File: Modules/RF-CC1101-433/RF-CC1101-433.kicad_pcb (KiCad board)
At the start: 4 copper layers, 25 parts, among them J3 SMA edge-mount 50R, U4 CC1101RGPR, Y2 26.000MHz CL=10pF

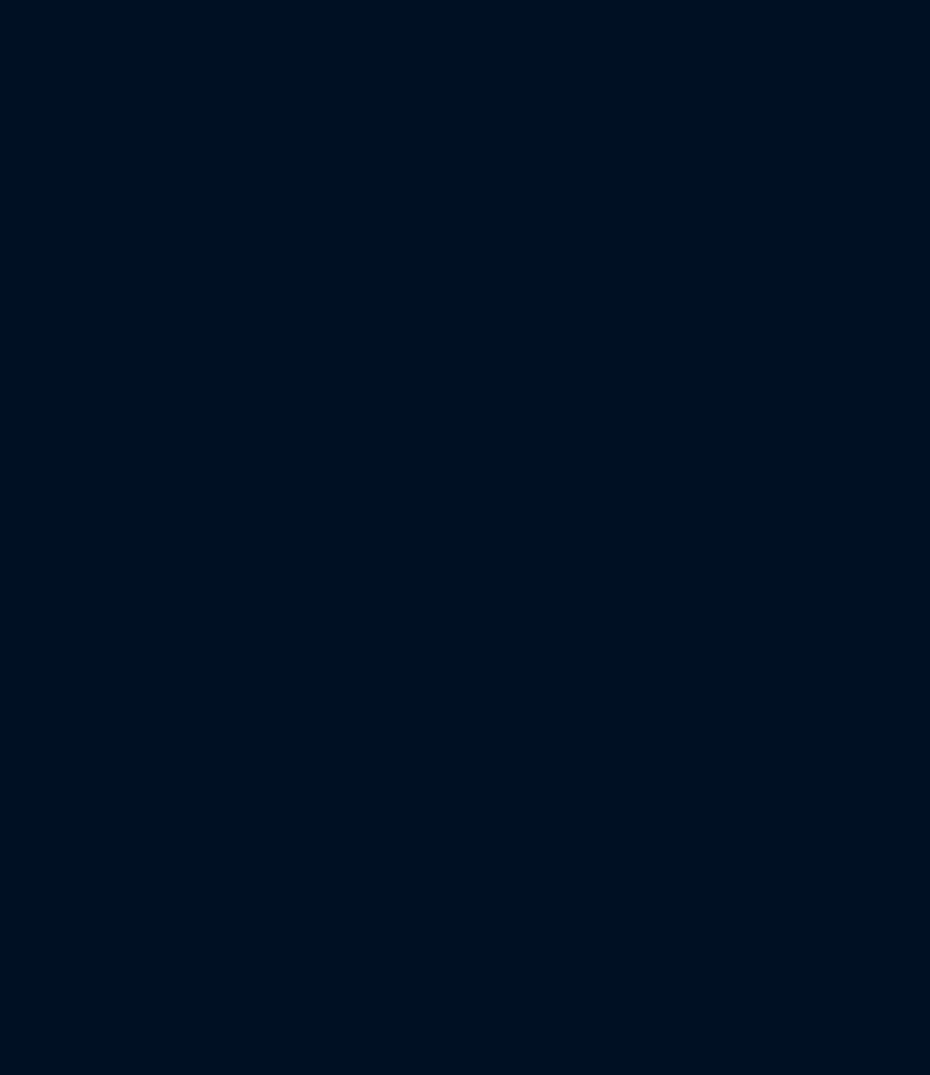
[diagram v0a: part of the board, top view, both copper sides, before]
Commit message: Add the base zones to five module boards
Whole-board zones for USBC, Buck, PowerMux, MCU and RF, written by file
before each board is opened. RF In1 carries a notch under J3 pad 1. Power
polygons become wide tracks during layout, because add_copper_pour cannot
set a zone priority.

Co-Authored-By: Claude Opus 5.5 (1M context) <noreply@anthropic.com>
Claude-Session: https://claude.ai/code/session_01ErAAfkmF4h3T5yfrw21utF
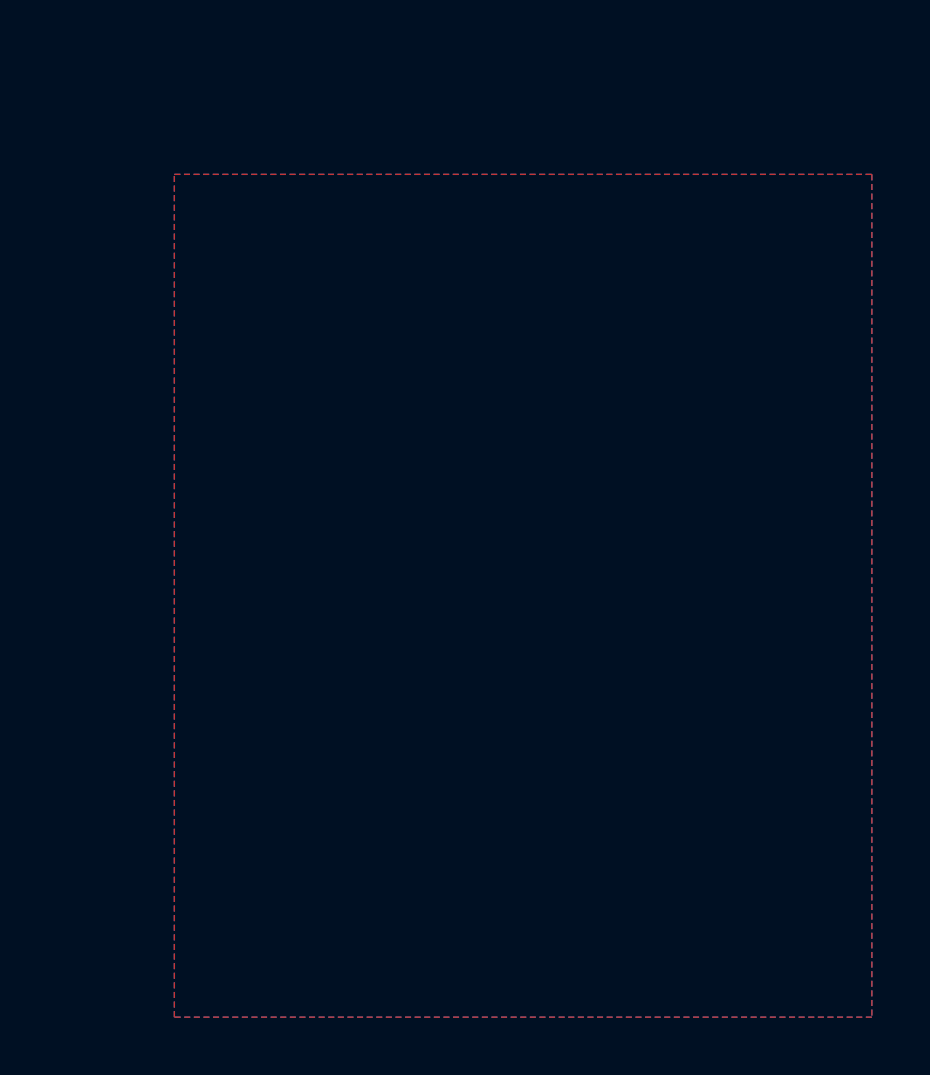
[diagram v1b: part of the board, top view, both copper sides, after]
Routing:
- added copper zone on B.Cu, net GND
- added copper zone on F.Cu, net GND
- added copper zone on In1.Cu, net GND
- added copper zone on In2.Cu, net GND
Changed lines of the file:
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@@
 	)
 	(embedded_fonts no)
-)
+  (zone (net 0) (net_name "GND") (layer "F.Cu")
+    (hatch edge 0.508)
+    (connect_pads (clearance 0.2))
+    (min_thickness 0.25)
+    (fill yes)
+    (polygon (pts
+      (xy 100.5 100.5)
+      (xy 124.5 100.5)
+      (xy 124.5 129.5)
+      (xy 100.5 129.5)
+    ))
+  )
+  (zone (net 0) (net_name "GND") (layer "In1.Cu")
+    (hatch edge 0.508)
+    (connect_pads (clearance 0.2))
+    (min_thickness 0.25)
+    (fill yes)
+    (polygon (pts
+      (xy 100.5 100.5)
+      (xy 110.38 100.5)
+      (xy 110.38 105.33)
+      (xy 112.38 105.33)
+      (xy 112.38 100.5)
+      (xy 124.5 100.5)
+      (xy 124.5 129.5)
+      (xy 100.5 129.5)
+    ))
+  )
+  (zone (net 0) (net_name "GND") (layer "In2.Cu")
+    (hatch edge 0.508)
+    (connect_pads (clearance 0.2))
+    (min_thickness 0.25)
+    (fill yes)
+    (polygon (pts
+      (xy 100.5 100.5)
+      (xy 124.5 100.5)
+      (xy 124.5 129.5)
+      (xy 100.5 129.5)
+    ))
+  )
+  (zone (net 0) (net_name "GND") (layer "B.Cu")
+    (hatch edge 0.508)
+    (connect_pads (clearance 0.2))
+    (min_thickness 0.25)
+    (fill yes)
+    (polygon (pts
+      (xy 100.5 100.5)
+      (xy 124.5 100.5)
+      (xy 124.5 129.5)
+      (xy 100.5 129.5)
+    ))
+  ))

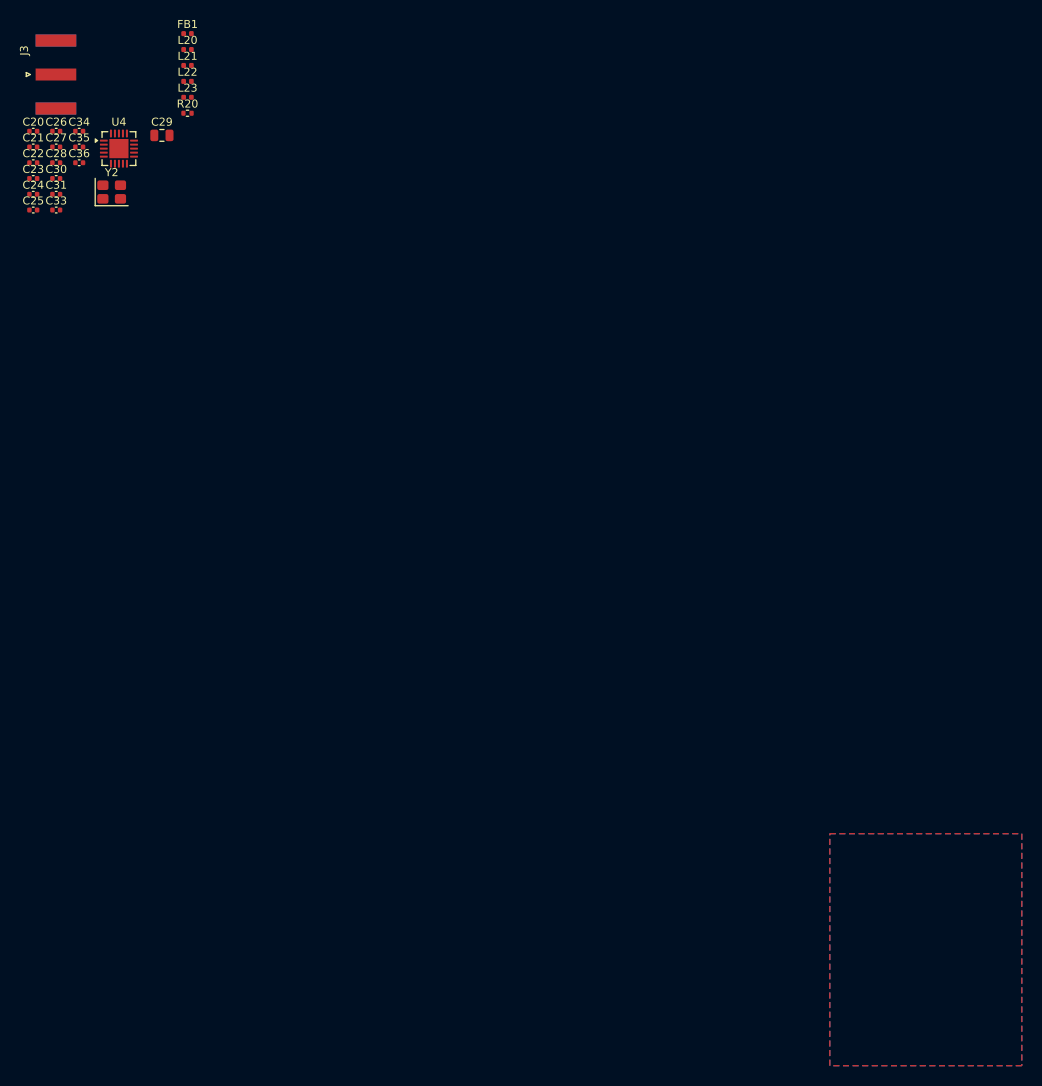
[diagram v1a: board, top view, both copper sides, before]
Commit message: Lay out the RF-CC1101-433 module
25 x 30 mm, 4 layers. The SWRR046 match chain runs in one straight column
from U4 to J3 on the top edge. The bare 50 ohm feed from C35 to J3 is about
1.0 mm at 0.17 mm. GND stitch vias line both sides of the chain, and each
shunt pad has its own GND via. VDD runs on F.Cu with a five-via B.Cu jumper
tree, as SWRR046 uses its bottom layer, clear of the chip and the match.
Five exposed-pad vias. C20 and C21 unchanged at 12 pF and 15 pF.

DRC: 0 errors, 0 unconnected, 0 parity. The 7 track_dangling warnings are
the 7 interface stubs. Canary 149 to 661. One lib_footprint_mismatch on U4
for GUI batch 2.

Open for the fab: the exposed-pad vias sit inside the pad mask opening, so
they need plugging.

Also add GUI batch 2 to docs/Layout-Batch-Runbook.md.

Co-Authored-By: Claude Opus 5.5 (1M context) <noreply@anthropic.com>
Claude-Session: https://claude.ai/code/session_01ErAAfkmF4h3T5yfrw21utF
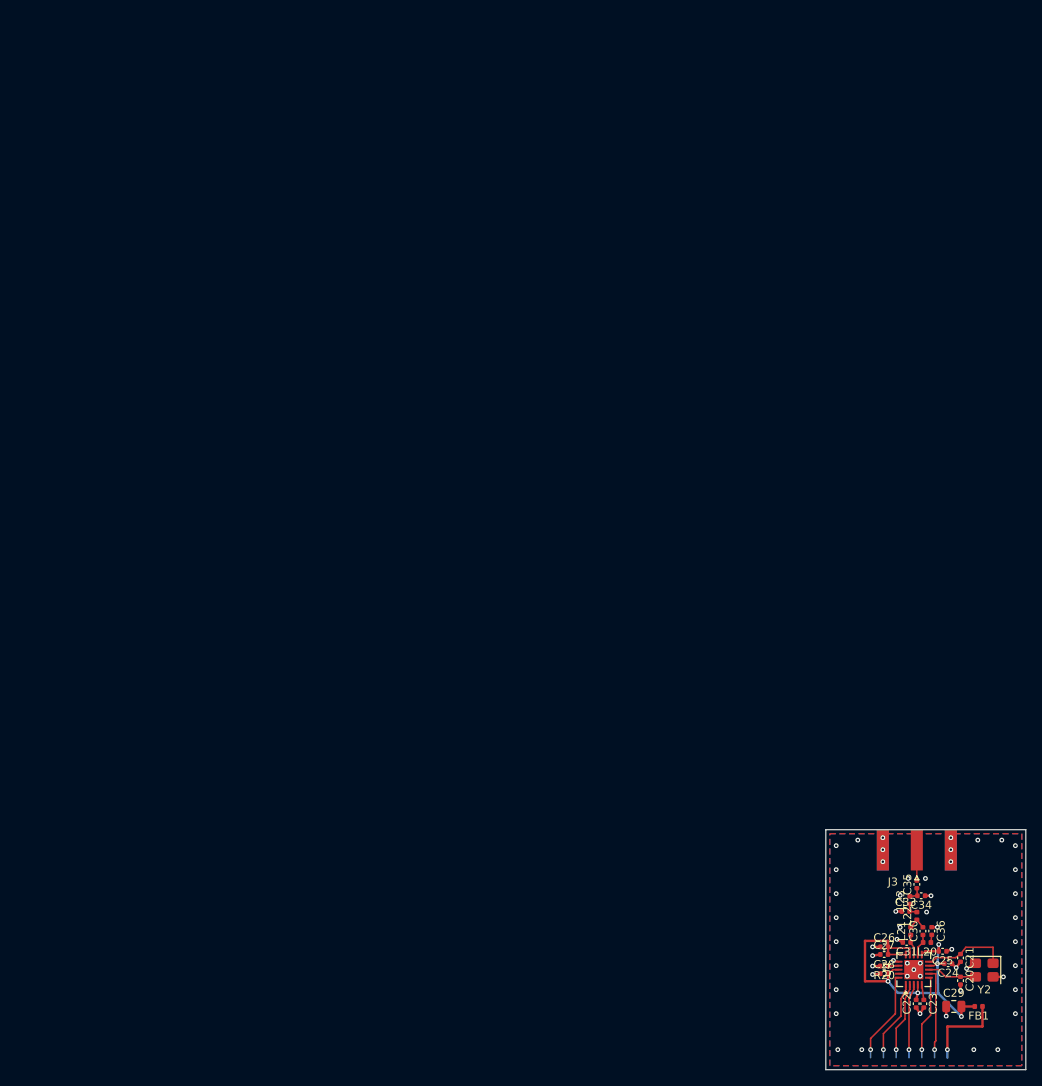
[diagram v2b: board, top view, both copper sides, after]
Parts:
- moved C20 157.2 mm to (116.8, 118.9), turned to -90 degrees
- moved FB1 156.7 mm to (119.1, 122.1), turned to 180 degrees
- moved C21 154.0 mm to (116.8, 116.0), turned to -90 degrees
- moved C22 152.4 mm to (111.3, 121.8), turned to 90 degrees
- moved C23 151.8 mm to (112.2, 121.8), turned to -90 degrees
- moved C24 149.4 mm to (115.3, 116.8), turned to 180 degrees
- moved C29 147.2 mm to (116.0, 122.1)
- moved C25 146.6 mm to (114.6, 115.2), turned to 180 degrees
- moved Y2 146.1 mm to (119.8, 117.5), turned to 180 degrees
- moved C26 145.3 mm to (107.3, 114.7)
- moved L20 144.9 mm to (112.7, 114.1), turned to 180 degrees
- moved C28 144.9 mm to (107.3, 118.0)
- moved J3 144.8 mm to (111.4, 102.6), turned to 90 degrees
- moved C27 144.6 mm to (107.3, 115.6)
- moved C30 143.5 mm to (112.1, 112.7), turned to 90 degrees
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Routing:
- net /VDD_CC1101: track 0.00 -> 47.9 mm, vias 0 -> 5
- net GND: track 0.00 -> 17.5 mm, vias 0 -> 55
- net /CC1101_MOSI: track 0.00 -> 11.7 mm, vias 0 -> 1
- net /CC1101_CS: track 0.00 -> 11.4 mm, vias 0 -> 1
- net /XTAL2: track 0.00 -> 10.8 mm
- net /+3V3_RF: track 0.00 -> 10.8 mm, vias 0 -> 1
- net /CC1101_GDO0_TX: track 0.00 -> 10.7 mm, vias 0 -> 1
- net /CC1101_SCK: track 0.00 -> 10.2 mm, vias 0 -> 1
- net /CC1101_MISO: track 0.00 -> 9.71 mm, vias 0 -> 1
- net /CC1101_GDO2_RX: track 0.00 -> 9.25 mm, vias 0 -> 1
- net /XTAL1: track 0.00 -> 6.19 mm
- net /ANT_433: track 0.00 -> 3.80 mm
- net /RF_P: track 0.00 -> 2.75 mm
- net /RF_N: track 0.00 -> 2.57 mm
- net /BALUN_OUT: track 0.00 -> 2.41 mm
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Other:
- board outline added: 25 x 30 mm
- board text added: "+3V3_RF"
- board text added: "CS"
- board text added: "GDO0_TX"
- board text added: "GDO2_RX"
- board text added: "GND"
- board text added: "MISO"
- board text added: "MOSI"
- board text added: "SCK"

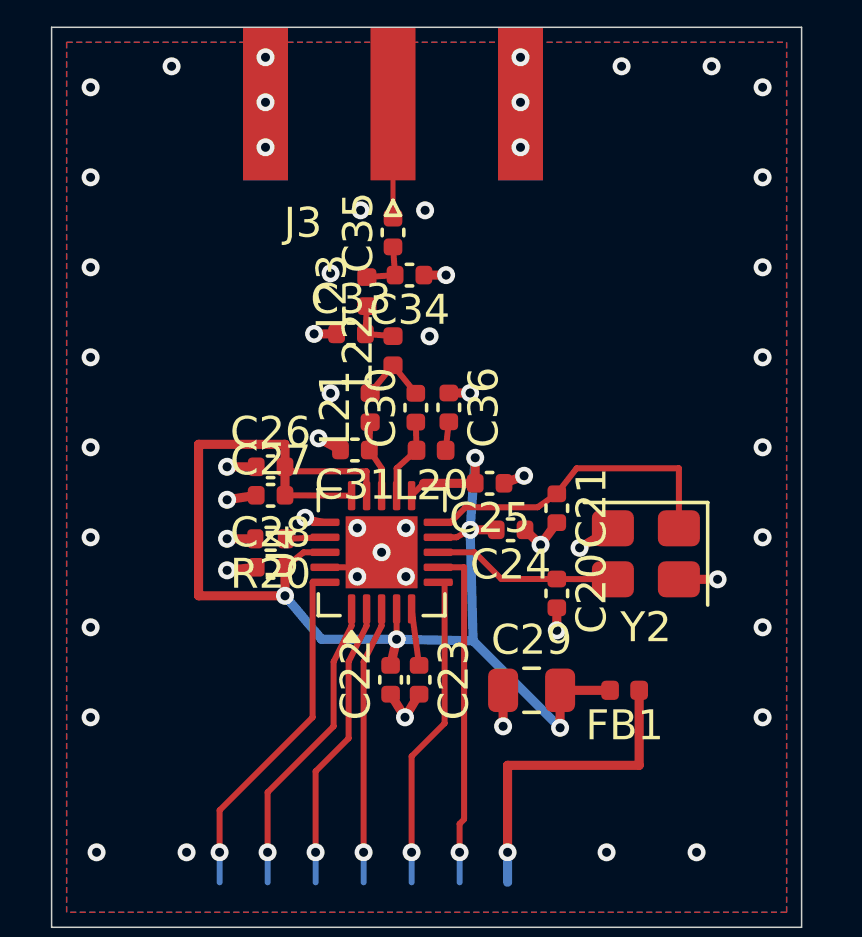
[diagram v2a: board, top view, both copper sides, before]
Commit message: Restore footprints and move passive references to F.Fab
GUI batch 2a on all eight module boards. Update Footprints from Library
restores the (units) blocks that Konnect IPC writes dropped: U10, U1, SW1,
SW2 and U4 no longer report lib_footprint_mismatch. Reference designators of
C, R, L, FB, D, Y and TP parts move to F.Fab. U, J and SW stay on the silk.

Every board: DRC 0 errors, 0 unconnected, 0 parity, the canary fires, and
track_dangling equals the interface stub count.

Co-Authored-By: Claude Opus 5.5 (1M context) <noreply@anthropic.com>
Claude-Session: https://claude.ai/code/session_01ErAAfkmF4h3T5yfrw21utF
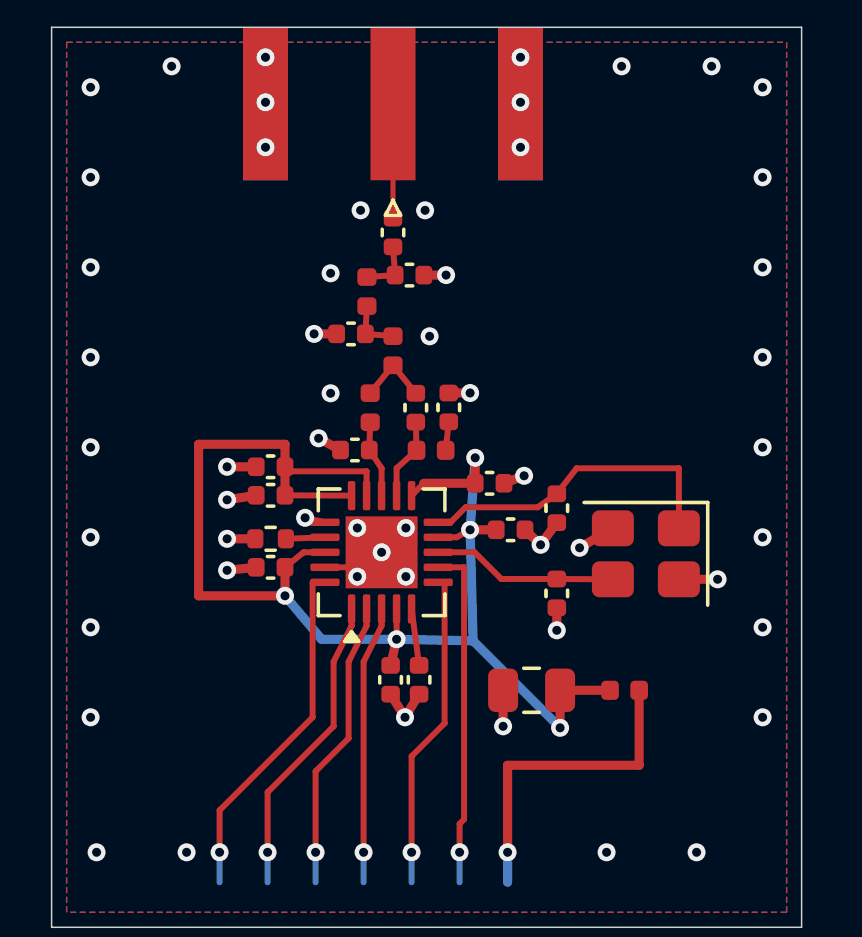
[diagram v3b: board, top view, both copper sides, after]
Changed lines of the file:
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@@
 		(property "Reference" "L21"
 			(at 0 -1.17 90)
-			(layer "F.SilkS")
+			(layer "F.Fab")
 			(effects
 				(font
@@
 		(property "Reference" "C20"
 			(at 0 -1.16 -90)
-			(layer "F.SilkS")
+			(layer "F.Fab")
 			(effects
 				(font
@@
 		(property "Reference" "L23"
 			(at 0 -1.17 90)
-			(layer "F.SilkS")
+			(layer "F.Fab")
 			(effects
 				(font
@@
 		(property "Reference" "C29"
 			(at 0 -1.68 0)
-			(layer "F.SilkS")
+			(layer "F.Fab")
 			(effects
 				(font
@@
 		(property "Reference" "FB1"
 			(at 0 -1.17 180)
-			(layer "F.SilkS")
+			(layer "F.Fab")
 			(effects
 				(font
@@
 		(property "Reference" "C28"
 			(at 0 -1.16 0)
-			(layer "F.SilkS")
+			(layer "F.Fab")
 			(effects
 				(font
@@
 		(property "Reference" "C26"
 			(at 0 -1.16 0)
-			(layer "F.SilkS")
+			(layer "F.Fab")
 			(effects
 				(font
@@
 		(property "Reference" "J3"
 			(at -3.96 -3 180)
-			(layer "F.SilkS")
+			(layer "F.Fab")
 			(effects
 				(font
@@
 		(property "Reference" "C27"
 			(at 0 -1.16 0)
-			(layer "F.SilkS")
+			(layer "F.Fab")
 			(effects
 				(font
@@
 		(property "Reference" "C30"
 			(at 0 -1.16 90)
-			(layer "F.SilkS")
+			(layer "F.Fab")
 			(effects
 				(font
@@
 		(property "Reference" "C25"
 			(at 0 -1.16 180)
-			(layer "F.SilkS")
+			(layer "F.Fab")
 			(effects
 				(font
@@
 		(property "Reference" "C35"
 			(at 0 -1.16 90)
-			(layer "F.SilkS")
+			(layer "F.Fab")
 			(effects
 				(font
@@
 		(property "Reference" "C36"
 			(at 0 -1.16 -90)
-			(layer "F.SilkS")
+			(layer "F.Fab")
 			(effects
 				(font
@@
 		(property "Reference" "U4"
 			(at 0 -3.33 90)
-			(layer "F.SilkS")
+			(layer "F.Fab")
 			(effects
 				(font
@@
 			(at 0 0 90)
 			(size 2.4 2.4)
+			(property pad_prop_heatsink)
 			(layers "F.Cu" "F.Mask")
 			(net "GND")
@@
 		(property "Reference" "L22"
 			(at 0 -1.17 90)
-			(layer "F.SilkS")
+			(layer "F.Fab")
 			(effects
 				(font
@@
 		(property "Reference" "Y2"
 			(at 0 -2.45 180)
-			(layer "F.SilkS")
+			(layer "F.Fab")
 			(effects
 				(font
@@
 		(property "Reference" "C21"
 			(at 0 -1.16 -90)
-			(layer "F.SilkS")
+			(layer "F.Fab")
 			(effects
 				(font
@@
 		(property "Reference" "C22"
 			(at 0 -1.16 90)
-			(layer "F.SilkS")
+			(layer "F.Fab")
 			(effects
 				(font
@@
 		(property "Reference" "C33"
 			(at 0 -1.16 0)
-			(layer "F.SilkS")
+			(layer "F.Fab")
 			(effects
 				(font
@@
 		(property "Reference" "C31"
 			(at 0 -1.16 180)
-			(layer "F.SilkS")
+			(layer "F.Fab")
 			(effects
 				(font
@@
 		(property "Reference" "R20"
 			(at 0 -1.17 180)
-			(layer "F.SilkS")
+			(layer "F.Fab")
 			(effects
 				(font
@@
 		(property "Reference" "L20"
 			(at 0 -1.17 180)
-			(layer "F.SilkS")
+			(layer "F.Fab")
 			(effects
 				(font
@@
 		(property "Reference" "C24"
 			(at 0 -1.16 180)
-			(layer "F.SilkS")
+			(layer "F.Fab")
 			(effects
 				(font
@@
 		(property "Reference" "C34"
 			(at 0 -1.16 180)
-			(layer "F.SilkS")
+			(layer "F.Fab")
 			(effects
 				(font
@@
 		(property "Reference" "C23"
 			(at 0 -1.16 -90)
-			(layer "F.SilkS")
+			(layer "F.Fab")
 			(effects
 				(font
